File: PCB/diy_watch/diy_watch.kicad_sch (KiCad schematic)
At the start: 49 parts, among them IC1 W25Q16JVUXIQ, J1 USB_B_Micro, SW1 SW_Push, U1 FTE-2CA-V-T/R, U2 DS3231MZ, U3 RP2040, U7 XC6210B332MR, U8 LTC4071EMS8E_PBF, Y1 12MHz_crystal

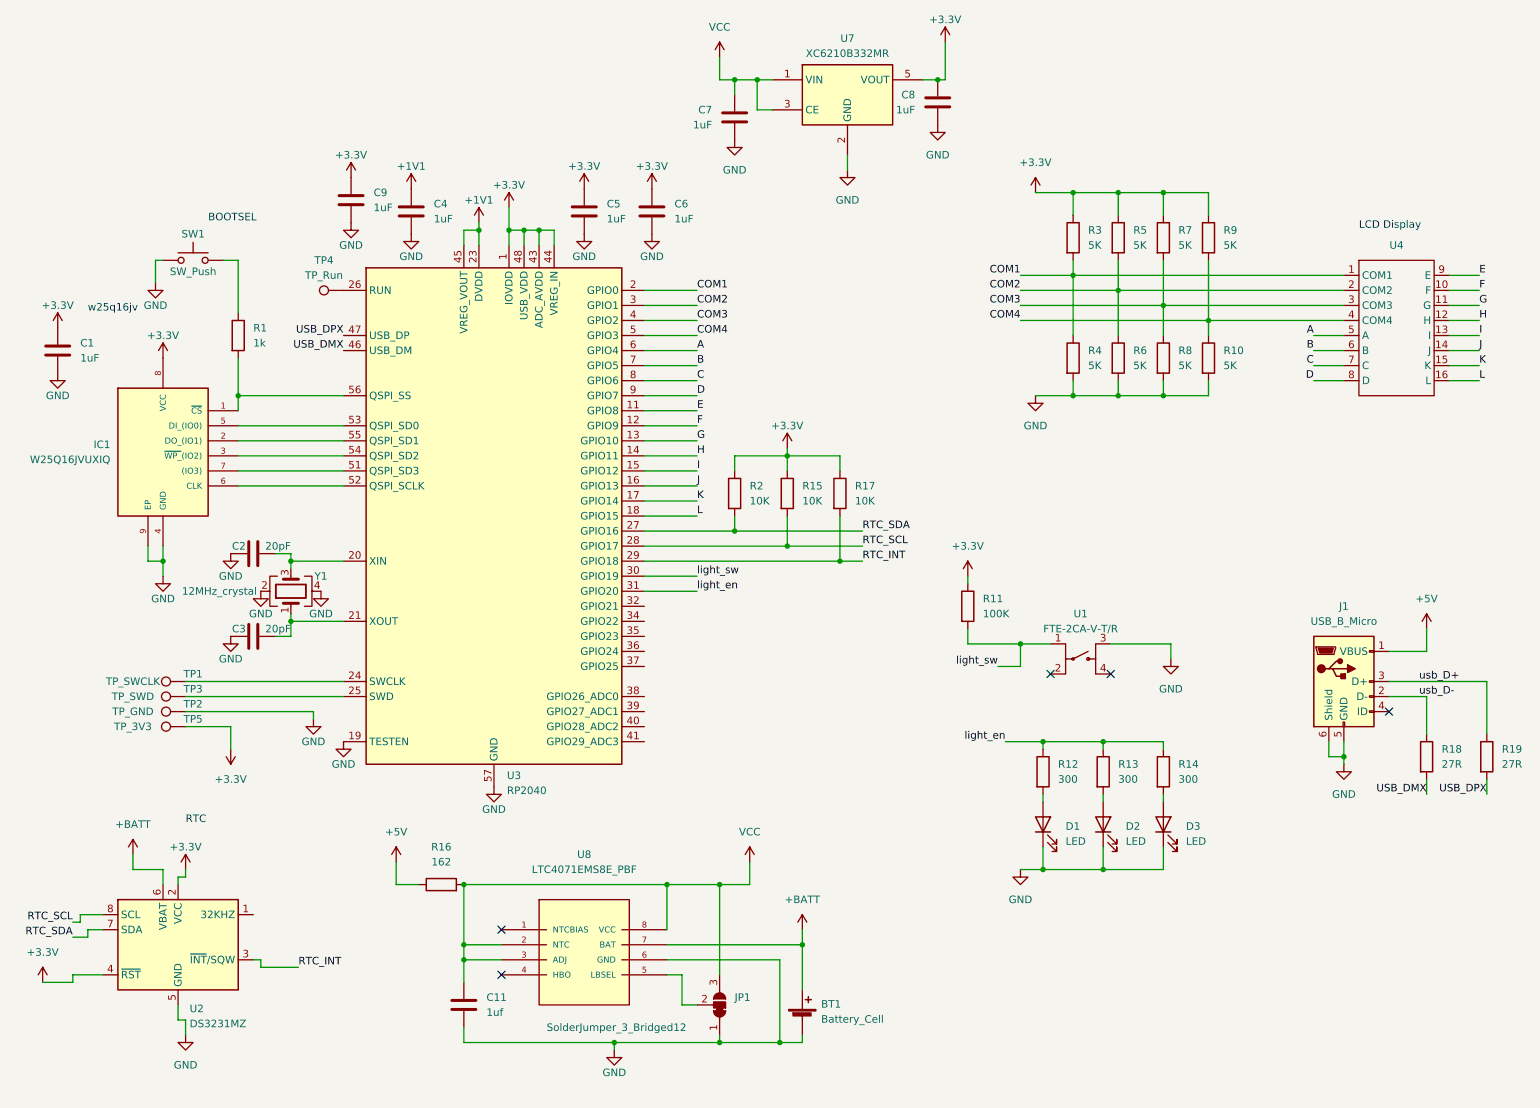
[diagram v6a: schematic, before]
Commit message: Updating to 4 layer board Adding missing caps to schematic Updating pcb with schematic fixes
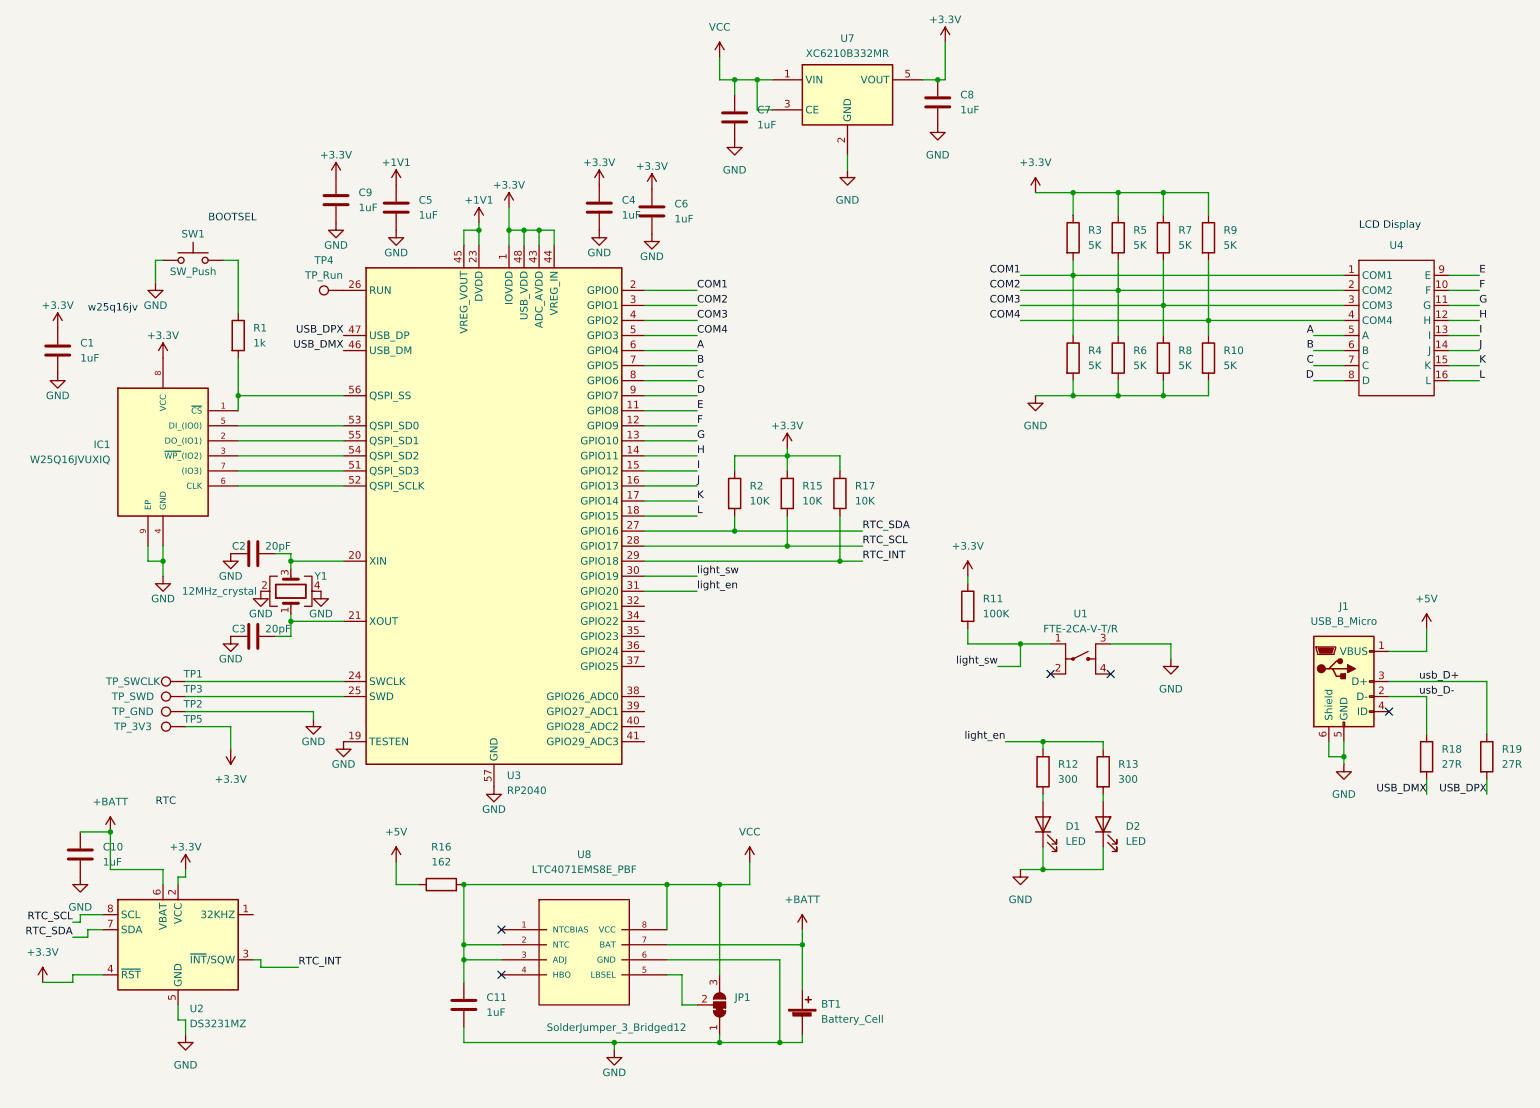
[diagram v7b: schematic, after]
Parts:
- removed D3: LED, LED_SMD:LED_0805_2012Metric, symbol Device:LED
- removed R14: 300, LED_SMD:LED_0402_1005Metric, symbol Device:R
- added C10: 1uF, Capacitor_SMD:C_0402_1005Metric, symbol Device:C
- C1, C4, C5, C6, C7, C8, C9: JLCPCB Part (none) -> C52923
- C11: value 1uf -> 1uF; JLCPCB Part (none) -> C52923
- C2, C3: JLCPCB Part (none) -> C1554
- IC1: JLCPCB Part (none) -> C2843335
- R11: JLCPCB Part (none) -> C25741
- Y1: JLCPCB Part (none) -> C9002; jlc# C9002 -> (none)
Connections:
- net +1V1: now also C5.1; no longer C4.1
- net +3.3V: now also C4.1; no longer C5.1
- net +BATT: now also C10.1
- net GND: now also C10.2

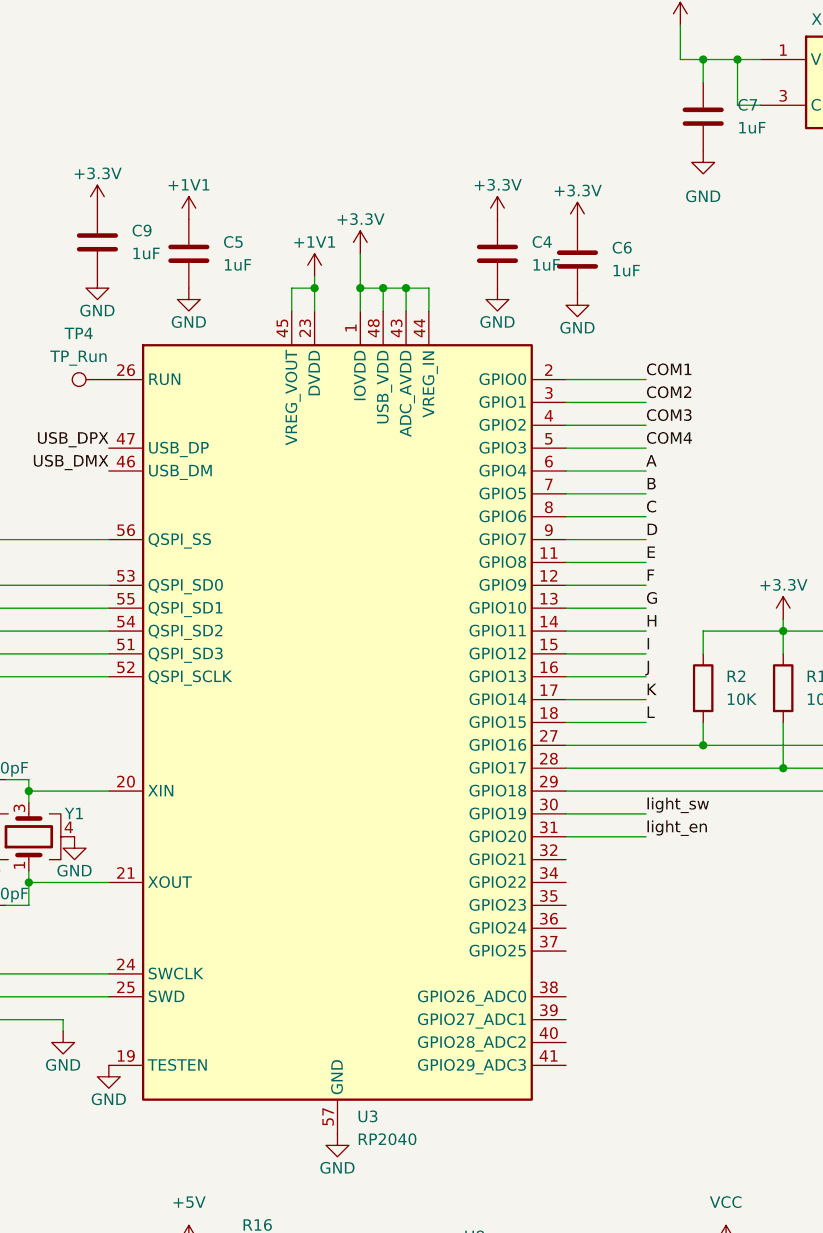
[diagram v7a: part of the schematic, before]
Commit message: Fixing ERC and DRC errors
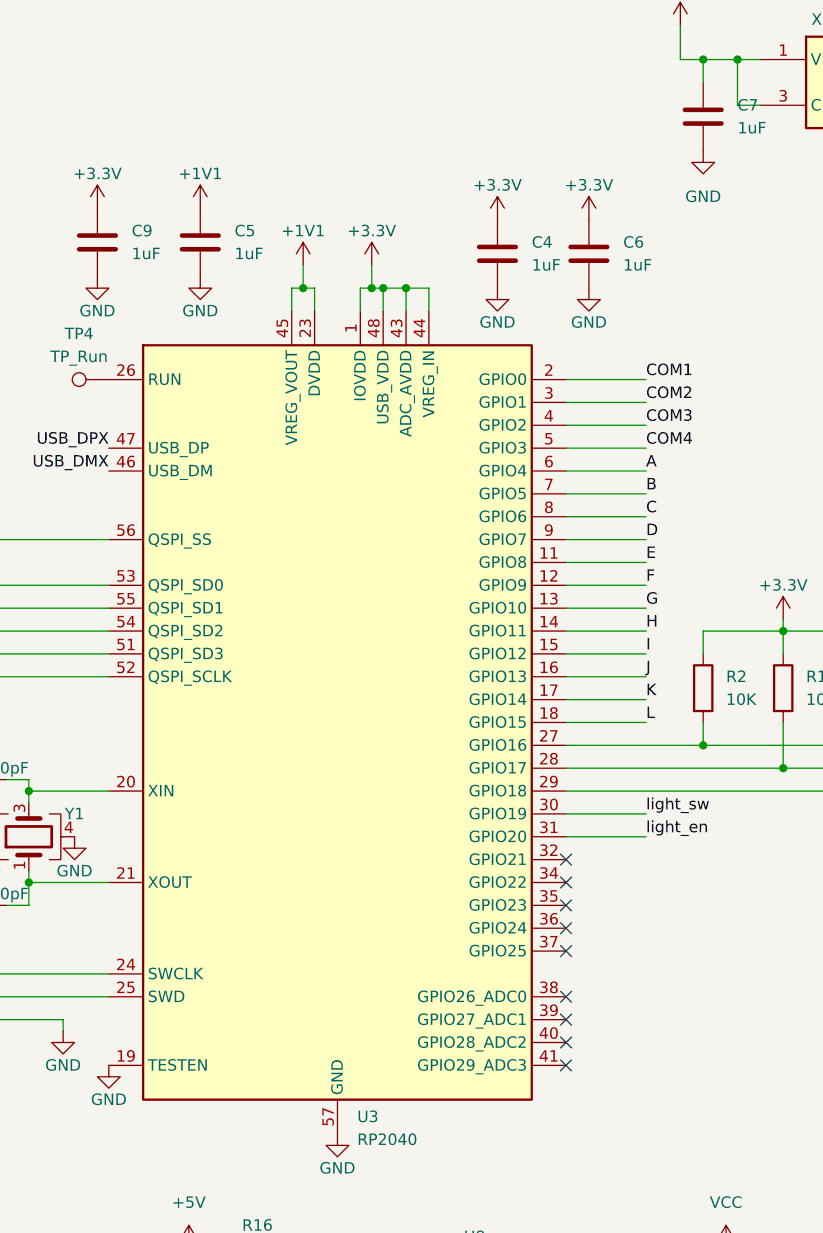
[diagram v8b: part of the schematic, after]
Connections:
- no-connect marks 5 -> 14
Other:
- moved on the sheet: C5, C6
